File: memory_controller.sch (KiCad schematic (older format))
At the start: 39 parts, among them SW1 SW_DIP_x03, U14 STM32F407VGTx

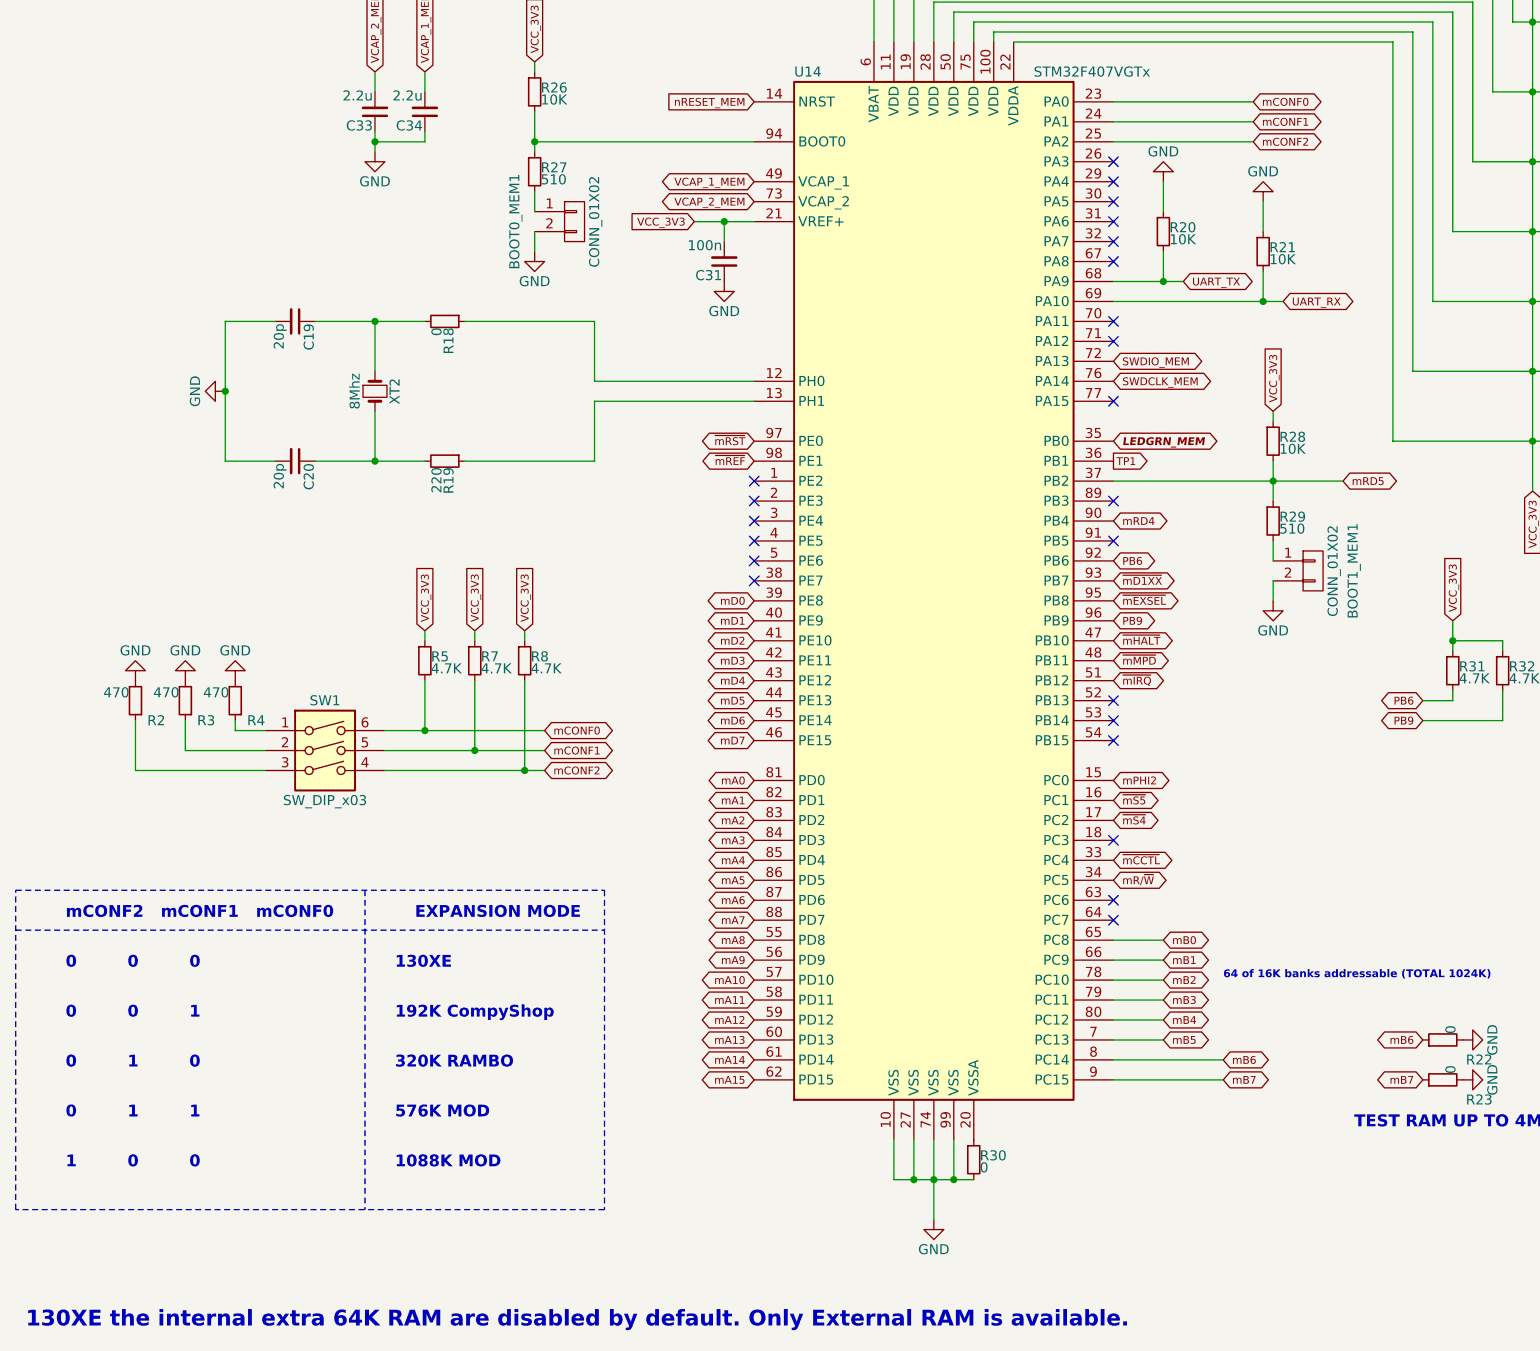
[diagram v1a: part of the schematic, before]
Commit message: Optimized for 8 bit access. Added a configuration option. A31 on connector is 5VDC. Not used here
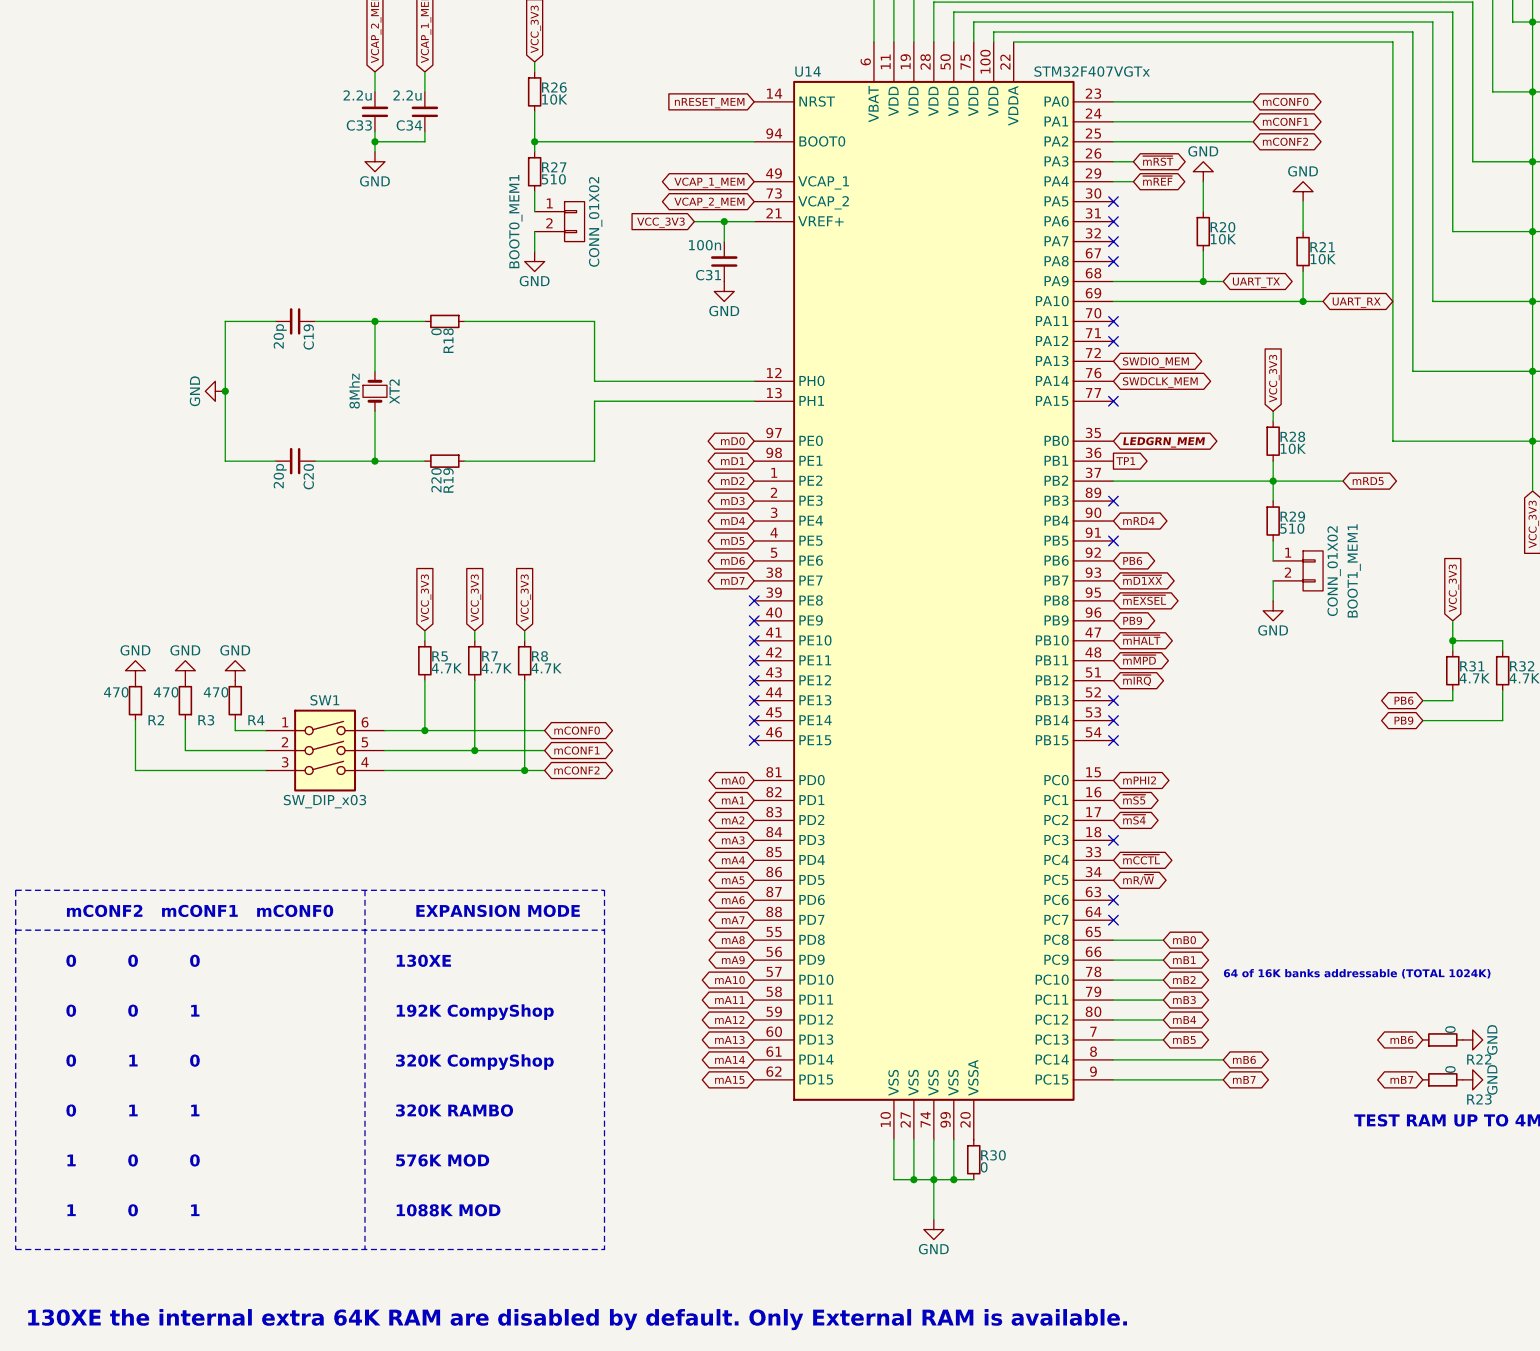
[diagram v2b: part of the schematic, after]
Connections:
- net mD0: now also U14.97 (PE0); no longer U14.39 (PE8)
- net mD1: now also U14.98 (PE1); no longer U14.40 (PE9)
- net mD2: now also U14.1 (PE2); no longer U14.41 (PE10)
- net mD3: now also U14.2 (PE3); no longer U14.42 (PE11)
- net mD4: now also U14.3 (PE4); no longer U14.43 (PE12)
- net mD5: now also U14.4 (PE5); no longer U14.44 (PE13)
- net mD6: now also U14.5 (PE6); no longer U14.45 (PE14)
- net mD7: now also U14.38 (PE7); no longer U14.46 (PE15)
- net ~mREF: now also U14.29 (PA4); no longer U14.98 (PE1)
- net ~mRST: now also U14.26 (PA3); no longer U14.97 (PE0)
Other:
- note added: "1 0 1"
- note added: "320K CompyShop"
- moved on the sheet: R20, R21

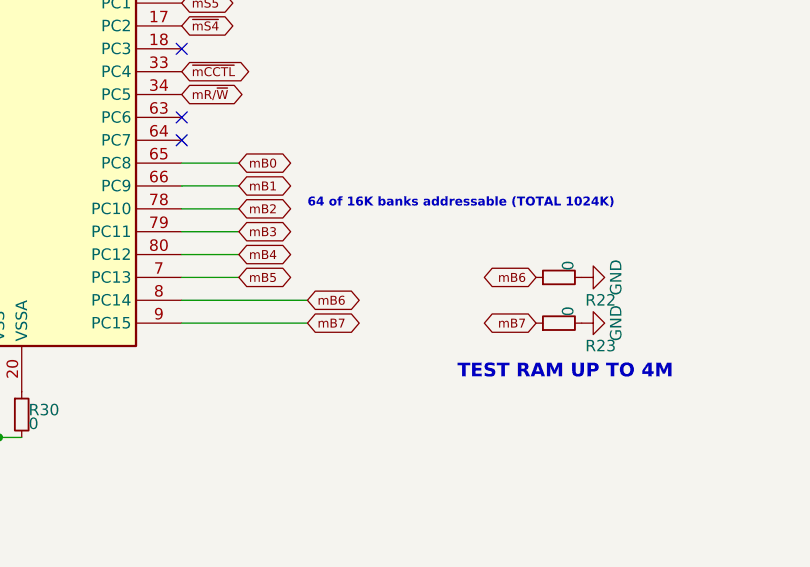
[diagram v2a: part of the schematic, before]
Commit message: Upgraded to a dual chip select for external SRAM. In this case up to 1536k can be addressable
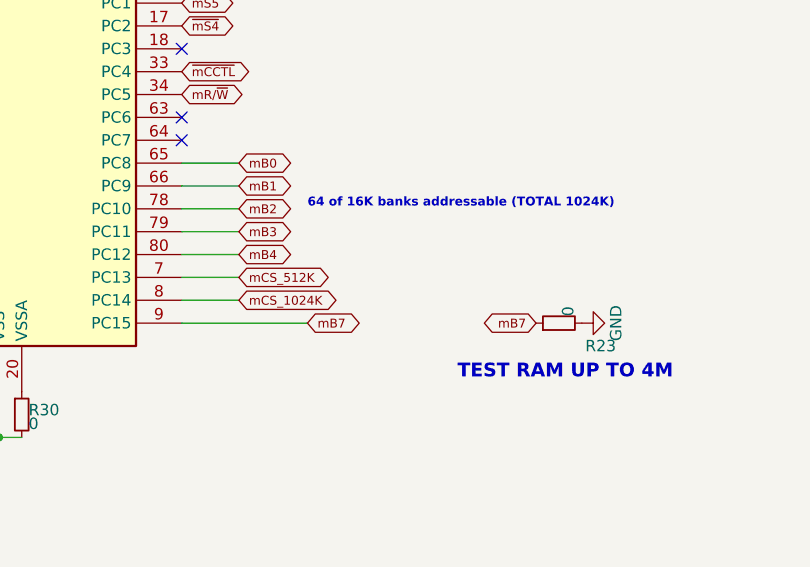
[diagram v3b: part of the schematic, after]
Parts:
- removed R22: 0, Resistors_SMD:R_1206_HandSoldering, symbol R_Small
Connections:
- net mB5 renamed mCS_512K
- net mB6 renamed mCS_1024K
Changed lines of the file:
@@
 Text GLabel 6450 5850 2    39   BiDi ~ 0
 mB4
-Text GLabel 6450 5950 2    39   BiDi ~ 0
-mB5
 Text Notes 6750 5650 0    39   ~ 8
 64 of 16K banks addressable (TOTAL 1024K)
-Text GLabel 6750 6050 2    39   BiDi ~ 0
-mB6
 Text GLabel 6750 6150 2    39   BiDi ~ 0
 mB7
@@
 $EndComp
 $Comp
-L R_Small R22
-U 1 1 5CA87774
-P 7850 5950
-F 0 "R22" V 7750 5700 50  0000 L CNN
-F 1 "0" H 7880 5910 50  0000 L CNN
-F 2 "Resistors_SMD:R_1206_HandSoldering" H 7850 5950 50  0001 C CNN
-F 3 "" H 7850 5950 50  0001 C CNN
-	1    7850 5950
-	0    -1   -1   0
-$EndComp
-$Comp
 L GND #PWR026
-U 1 1 5CA883BF
-P 7950 5950
-F 0 "#PWR026" H 7950 5700 50  0001 C CNN
-F 1 "GND" H 7950 5800 50  0000 C CNN
-F 2 "" H 7950 5950 50  0001 C CNN
-F 3 "" H 7950 5950 50  0001 C CNN
-	1    7950 5950
-	0    -1   -1   0
-$EndComp
-$Comp
-L GND #PWR027
 U 1 1 5CA8840A
 P 7950 6150
-F 0 "#PWR027" H 7950 5900 50  0001 C CNN
+F 0 "#PWR026" H 7950 5900 50  0001 C CNN
 F 1 "GND" H 7950 6000 50  0000 C CNN
 F 2 "" H 7950 6150 50  0001 C CNN
@@
 	0    -1   -1   0
 $EndComp
-Text GLabel 7750 5950 0    39   BiDi ~ 0
-mB6
 Text GLabel 7750 6150 0    39   BiDi ~ 0
 mB7
@@
 $EndComp
 $Comp
-L GND #PWR028
+L GND #PWR027
 U 1 1 5CBFC64D
 P 7000 3750
-F 0 "#PWR028" H 7000 3500 50  0001 C CNN
+F 0 "#PWR027" H 7000 3500 50  0001 C CNN
 F 1 "GND" H 7000 3600 50  0000 C CNN
 F 2 "" H 7000 3750 50  0001 C CNN
@@
 $EndComp
 $Comp
-L GND #PWR029
+L GND #PWR028
 U 1 1 5CBFD047
 P 3300 2000
-F 0 "#PWR029" H 3300 1750 50  0001 C CNN
+F 0 "#PWR028" H 3300 1750 50  0001 C CNN
 F 1 "GND" H 3300 1850 50  0000 C CNN
 F 2 "" H 3300 2000 50  0001 C CNN
@@
 $EndComp
 $Comp
-L GND #PWR030
+L GND #PWR029
 U 1 1 5CBFD69C
 P 4250 2150
-F 0 "#PWR030" H 4250 1900 50  0001 C CNN
+F 0 "#PWR029" H 4250 1900 50  0001 C CNN
 F 1 "GND" H 4250 2000 50  0000 C CNN
 F 2 "" H 4250 2150 50  0001 C CNN
@@
 $EndComp
 $Comp
-L GND #PWR031
+L GND #PWR030
 U 1 1 5CBFDC43
 P 2500 1500
-F 0 "#PWR031" H 2500 1250 50  0001 C CNN
+F 0 "#PWR030" H 2500 1250 50  0001 C CNN
 F 1 "GND" H 2500 1350 50  0000 C CNN
 F 2 "" H 2500 1500 50  0001 C CNN
@@
 $EndComp
 $Comp
-L GND #PWR032
+L GND #PWR031
 U 1 1 5CF3D4D8
 P 1800 4150
-F 0 "#PWR032" H 1800 3900 50  0001 C CNN
+F 0 "#PWR031" H 1800 3900 50  0001 C CNN
 F 1 "GND" H 1800 4000 50  0000 C CNN
 F 2 "" H 1800 4150 50  0001 C CNN
@@
 $EndComp
 $Comp
-L GND #PWR033
+L GND #PWR032
 U 1 1 5CF3D8CC
 P 1550 4150
-F 0 "#PWR033" H 1550 3900 50  0001 C CNN
+F 0 "#PWR032" H 1550 3900 50  0001 C CNN
 F 1 "GND" H 1550 4000 50  0000 C CNN
 F 2 "" H 1550 4150 50  0001 C CNN
@@
 $EndComp
 $Comp
-L GND #PWR034
+L GND #PWR033
 U 1 1 5CF3D9DA
 P 1300 4150
-F 0 "#PWR034" H 1300 3900 50  0001 C CNN
+F 0 "#PWR033" H 1300 3900 50  0001 C CNN
 F 1 "GND" H 1300 4000 50  0000 C CNN
 F 2 "" H 1300 4150 50  0001 C CNN
@@
 	6200 6150 6750 6150
 Wire Wire Line
-	6200 6050 6750 6050
-Wire Wire Line
 	6200 3150 7350 3150
 Wire Wire Line
@@
 NoConn ~ 4400 3850
 NoConn ~ 4400 3750
+Text GLabel 6450 5950 2    39   BiDi ~ 0
+mCS_512K
+Text GLabel 6450 6050 2    39   BiDi ~ 0
+mCS_1024K
+Wire Wire Line
+	6200 6050 6450 6050
 $EndSCHEMATC

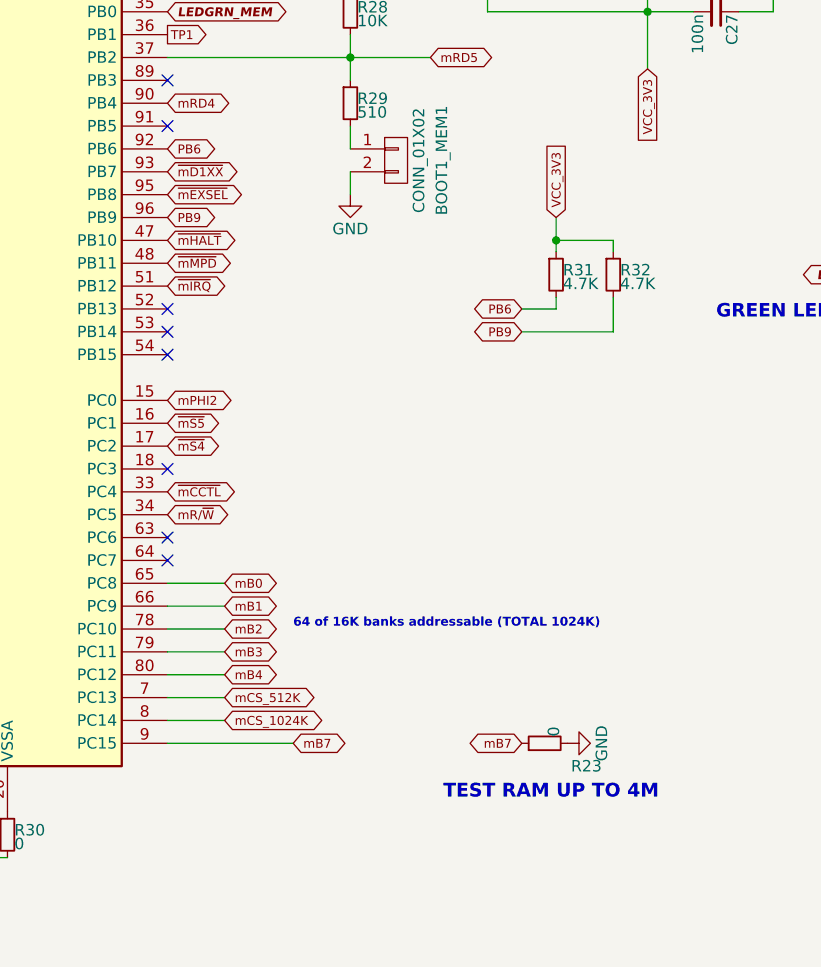
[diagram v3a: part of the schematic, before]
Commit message: Added nOE and nWE from the GPIOs
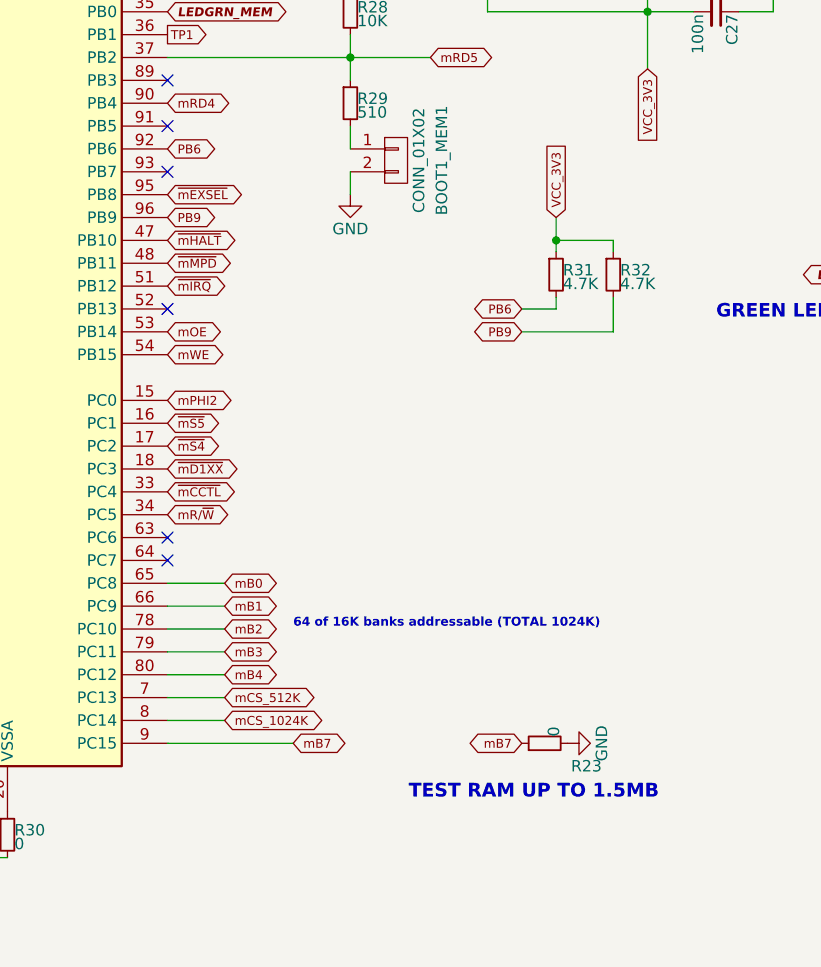
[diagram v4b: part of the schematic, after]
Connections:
- net ~mD1XX: now also U14.18 (PC3); no longer U14.93 (PB7)
- net mOE: now reaches U14.53 (PB14)
- net mWE: now reaches U14.54 (PB15)
- no-connect marks 23 -> 21
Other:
- note added: "TEST RAM UP TO 1.5MB"
- note removed: "TEST RAM UP TO 4M"
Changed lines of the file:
@@
 $EndComp
 $Comp
-L GND #PWR020
+L GND #PWR017
 U 1 1 5CA87C43
 P 1750 2700
-F 0 "#PWR020" H 1750 2450 50  0001 C CNN
+F 0 "#PWR017" H 1750 2450 50  0001 C CNN
 F 1 "GND" H 1750 2550 50  0000 C CNN
 F 2 "" H 1750 2700 50  0001 C CNN
@@
 $EndComp
 $Comp
-L GND #PWR021
+L GND #PWR018
 U 1 1 5CA87C4B
 P 8850 1900
-F 0 "#PWR021" H 8850 1650 50  0001 C CNN
+F 0 "#PWR018" H 8850 1650 50  0001 C CNN
 F 1 "GND" H 8850 1750 50  0000 C CNN
 F 2 "" H 8850 1900 50  0001 C CNN
@@
 $EndComp
 $Comp
-L GND #PWR022
+L GND #PWR019
 U 1 1 5C42325A
 P 9950 3400
-F 0 "#PWR022" H 9950 3150 50  0001 C CNN
+F 0 "#PWR019" H 9950 3150 50  0001 C CNN
 F 1 "GND" H 9950 3250 50  0000 C CNN
 F 2 "" H 9950 3400 50  0001 C CNN
@@
 $EndComp
 $Comp
-L GND #PWR023
+L GND #PWR020
 U 1 1 5C4234AD
 P 5300 6850
-F 0 "#PWR023" H 5300 6600 50  0001 C CNN
+F 0 "#PWR020" H 5300 6600 50  0001 C CNN
 F 1 "GND" H 5300 6700 50  0000 C CNN
 F 2 "" H 5300 6850 50  0001 C CNN
@@
 NoConn ~ 6200 2450
 NoConn ~ 6200 2750
-NoConn ~ 6200 4950
 NoConn ~ 6200 5250
 NoConn ~ 6200 5350
@@
 $EndComp
 $Comp
-L GND #PWR024
+L GND #PWR021
 U 1 1 5CA875AF
 P 6650 1650
-F 0 "#PWR024" H 6650 1400 50  0001 C CNN
+F 0 "#PWR021" H 6650 1400 50  0001 C CNN
 F 1 "GND" H 6650 1500 50  0000 C CNN
 F 2 "" H 6650 1650 50  0001 C CNN
@@
 $EndComp
 $Comp
-L GND #PWR025
+L GND #PWR022
 U 1 1 5CA87680
 P 7150 1750
-F 0 "#PWR025" H 7150 1500 50  0001 C CNN
+F 0 "#PWR022" H 7150 1500 50  0001 C CNN
 F 1 "GND" H 7150 1600 50  0000 C CNN
 F 2 "" H 7150 1750 50  0001 C CNN
@@
 $EndComp
 $Comp
-L GND #PWR026
+L GND #PWR023
 U 1 1 5CA8840A
 P 7950 6150
-F 0 "#PWR026" H 7950 5900 50  0001 C CNN
+F 0 "#PWR023" H 7950 5900 50  0001 C CNN
 F 1 "GND" H 7950 6000 50  0000 C CNN
 F 2 "" H 7950 6150 50  0001 C CNN
@@
 mB7
 Text Notes 8350 6400 2    60   ~ 12
-TEST RAM UP TO 4M
+TEST RAM UP TO 1.5MB
 Text GLabel 6200 3050 2    39   Output ~ 0
 TP1
@@
 Text GLabel 6200 3950 2    39   BiDi ~ 0
 ~mHALT
-Text GLabel 6200 3650 2    39   BiDi ~ 0
+Text GLabel 6200 4950 2    39   BiDi ~ 0
 ~mD1XX
 Text GLabel 6200 3750 2    39   BiDi ~ 0
@@
 $EndComp
 $Comp
-L GND #PWR027
+L GND #PWR024
 U 1 1 5CBFC64D
 P 7000 3750
-F 0 "#PWR027" H 7000 3500 50  0001 C CNN
+F 0 "#PWR024" H 7000 3500 50  0001 C CNN
 F 1 "GND" H 7000 3600 50  0000 C CNN
 F 2 "" H 7000 3750 50  0001 C CNN
@@
 $EndComp
 $Comp
-L GND #PWR028
+L GND #PWR025
 U 1 1 5CBFD047
 P 3300 2000
-F 0 "#PWR028" H 3300 1750 50  0001 C CNN
+F 0 "#PWR025" H 3300 1750 50  0001 C CNN
 F 1 "GND" H 3300 1850 50  0000 C CNN
 F 2 "" H 3300 2000 50  0001 C CNN
@@
 $EndComp
 $Comp
-L GND #PWR029
+L GND #PWR026
 U 1 1 5CBFD69C
 P 4250 2150
-F 0 "#PWR029" H 4250 1900 50  0001 C CNN
+F 0 "#PWR026" H 4250 1900 50  0001 C CNN
 F 1 "GND" H 4250 2000 50  0000 C CNN
 F 2 "" H 4250 2150 50  0001 C CNN
@@
 $EndComp
 $Comp
-L GND #PWR030
+L GND #PWR027
 U 1 1 5CBFDC43
 P 2500 1500
-F 0 "#PWR030" H 2500 1250 50  0001 C CNN
+F 0 "#PWR027" H 2500 1250 50  0001 C CNN
 F 1 "GND" H 2500 1350 50  0000 C CNN
 F 2 "" H 2500 1500 50  0001 C CNN
@@
 	1    0    0    -1
 $EndComp
-NoConn ~ 6200 4450
 NoConn ~ 6200 3250
 Text GLabel 7350 3150 2    39   BiDi ~ 0
@@
 Text GLabel 6200 3350 2    39   BiDi ~ 0
 mRD4
-NoConn ~ 6200 4350
 NoConn ~ 6200 4250
 $Comp
@@
 $EndComp
 $Comp
-L GND #PWR031
+L GND #PWR028
 U 1 1 5CF3D4D8
 P 1800 4150
-F 0 "#PWR031" H 1800 3900 50  0001 C CNN
+F 0 "#PWR028" H 1800 3900 50  0001 C CNN
 F 1 "GND" H 1800 4000 50  0000 C CNN
 F 2 "" H 1800 4150 50  0001 C CNN
@@
 $EndComp
 $Comp
-L GND #PWR032
+L GND #PWR029
 U 1 1 5CF3D8CC
 P 1550 4150
-F 0 "#PWR032" H 1550 3900 50  0001 C CNN
+F 0 "#PWR029" H 1550 3900 50  0001 C CNN
 F 1 "GND" H 1550 4000 50  0000 C CNN
 F 2 "" H 1550 4150 50  0001 C CNN
@@
 $EndComp
 $Comp
-L GND #PWR033
+L GND #PWR030
 U 1 1 5CF3D9DA
 P 1300 4150
-F 0 "#PWR033" H 1300 3900 50  0001 C CNN
+F 0 "#PWR030" H 1300 3900 50  0001 C CNN
 F 1 "GND" H 1300 4000 50  0000 C CNN
 F 2 "" H 1300 4150 50  0001 C CNN
@@
 Wire Wire Line
 	6200 6050 6450 6050
+Text GLabel 6200 4350 2    39   BiDi ~ 0
+mOE
+Text GLabel 6200 4450 2    39   BiDi ~ 0
+mWE
+NoConn ~ 6200 3650
 $EndSCHEMATC
